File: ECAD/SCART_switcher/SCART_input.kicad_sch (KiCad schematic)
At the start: 12 parts, among them Q1 BC847, Q2 BC847, U1 74AHC1G14

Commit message: progressed ecad
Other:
- note added: "(*1) FUNCTION pin has the following signaling: Level 0: 0 V to +2 V (SCART off) Level 1A: +4.5 V to +7 V (SCART on, 16:9) Level 1B: +9.5 V to +12 V (SCART on) The circuit doesn't distinguish between levels 1A and 1B as these are frequently not respected in consumer products. This way it is simpler to default to 4:3 format and if needed manualy adjust the TV to 16:9."
- note removed: "(*1) FUNCTION pin has the following signaling: Level 0: 0 V to +2 V (SCART off) Level 1A: +4.5 V to +7 V (SCART on, 16:9) Level 1B: +9.5 V to +12 V (SCART on)"
- moved on the sheet: C1, D1, Q1, R2, R3, R?, U1

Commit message: progressed ecad
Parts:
- J?: footprint SCART:SCART-F -> Connector_SCART:SCART-F
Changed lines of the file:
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@@
       (effects (font (size 1.27 1.27)))
     )
-    (property "Footprint" "SCART:SCART-F" (at 90.17 69.85 0)
+    (property "Footprint" "Connector_SCART:SCART-F" (at 90.17 69.85 0)
       (effects (font (size 1.27 1.27)) hide)
     )

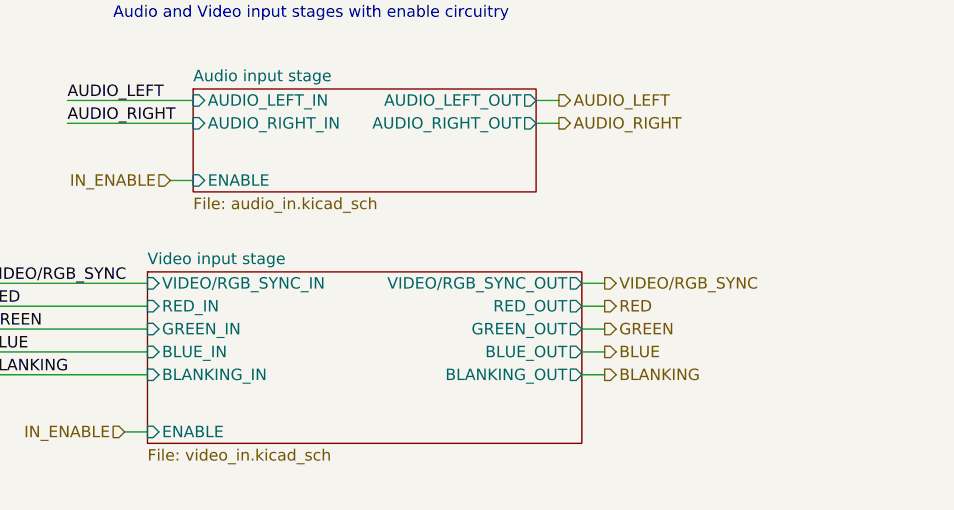
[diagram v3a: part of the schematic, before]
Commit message: ERC fixes.
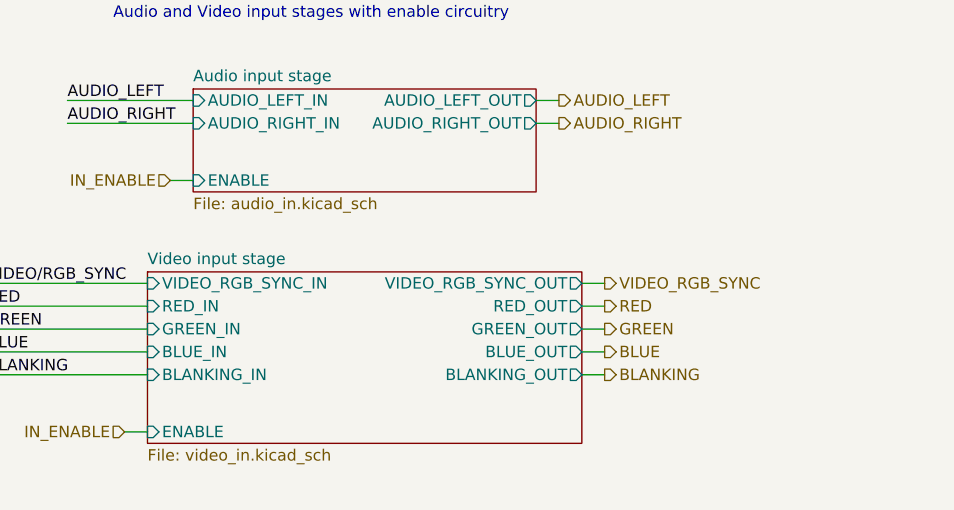
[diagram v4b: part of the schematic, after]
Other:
- sheet Video input stage ports: added VIDEO_RGB_SYNC_IN, VIDEO_RGB_SYNC_OUT; removed VIDEO/RGB_SYNC_IN, VIDEO/RGB_SYNC_OUT
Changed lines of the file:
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@@
     (effects (font (size 1.27 1.27)) (justify left))
   )
-  (hierarchical_label "VIDEO{slash}RGB_SYNC" (shape output) (at 118.11 158.75 0) (fields_autoplaced)
+  (hierarchical_label "VIDEO_RGB_SYNC" (shape output) (at 118.11 158.75 0) (fields_autoplaced)
     (effects (font (size 1.27 1.27)) (justify left))
   )
@@
         (path "/8cd08eb5-4755-4ef5-8eeb-77fd9974b180/f71a1287-269d-4354-9179-cb80a7e1dbca"
           (reference "#PWR0169") (unit 1)
-        )
-      )
-    )
-  )
-  (symbol (lib_id "power:GND") (at 228.6 69.85 0) (unit 1)
-    (in_bom yes) (on_board yes) (dnp no) (fields_autoplaced)
-    (property "Reference" "#PWR012" (at 228.6 76.2 0)
-      (effects (font (size 1.27 1.27)) hide)
-    )
-    (property "Value" "GND" (at 228.6 74.93 0)
-      (effects (font (size 1.27 1.27)))
-    )
-    (property "Footprint" "" (at 228.6 69.85 0)
-      (effects (font (size 1.27 1.27)) hide)
-    )
-    (property "Datasheet" "" (at 228.6 69.85 0)
-      (effects (font (size 1.27 1.27)) hide)
-    )
-    (pin "1")
-    (instances
-      (project "SCART_switcher"
-        (path "/8cd08eb5-4755-4ef5-8eeb-77fd9974b180/6e53f4c9-ed59-4c5d-ac8d-a66f0d353ca7"
-          (reference "#PWR012") (unit 1)
-        )
-        (path "/8cd08eb5-4755-4ef5-8eeb-77fd9974b180/8ea6db35-25d0-43bc-9de5-3ca23502dcdc"
-          (reference "#PWR043") (unit 1)
-        )
-        (path "/8cd08eb5-4755-4ef5-8eeb-77fd9974b180/272a4677-3ef2-418e-abc5-b29f59e726f9"
-          (reference "#PWR059") (unit 1)
-        )
-        (path "/8cd08eb5-4755-4ef5-8eeb-77fd9974b180/56b7edd2-65bf-4844-b6bd-3868b6562f83"
-          (reference "#PWR075") (unit 1)
-        )
-        (path "/8cd08eb5-4755-4ef5-8eeb-77fd9974b180/a066fdde-5f40-4269-95c1-258d611fd7cb"
-          (reference "#PWR091") (unit 1)
-        )
-        (path "/8cd08eb5-4755-4ef5-8eeb-77fd9974b180/ec158eb5-f3e0-409c-b64c-a90e3358941f"
-          (reference "#PWR0107") (unit 1)
-        )
-        (path "/8cd08eb5-4755-4ef5-8eeb-77fd9974b180/6c53b757-b2e6-4d60-b760-4a4a0f832c07"
-          (reference "#PWR0123") (unit 1)
-        )
-        (path "/8cd08eb5-4755-4ef5-8eeb-77fd9974b180/0223a704-ac47-44ed-9ba1-f418acceedb3"
-          (reference "#PWR0139") (unit 1)
-        )
-        (path "/8cd08eb5-4755-4ef5-8eeb-77fd9974b180/2ffa7ecd-d29d-4261-a577-43650ca26099"
-          (reference "#PWR0155") (unit 1)
-        )
-        (path "/8cd08eb5-4755-4ef5-8eeb-77fd9974b180/f71a1287-269d-4354-9179-cb80a7e1dbca"
-          (reference "#PWR0171") (unit 1)
         )
       )
@@
     )
   )
+  (symbol (lib_id "power:GND") (at 228.6 69.85 0) (unit 1)
+    (in_bom yes) (on_board yes) (dnp no) (fields_autoplaced)
+    (property "Reference" "#PWR012" (at 228.6 76.2 0)
+      (effects (font (size 1.27 1.27)) hide)
+    )
+    (property "Value" "GND" (at 228.6 74.93 0)
+      (effects (font (size 1.27 1.27)))
+    )
+    (property "Footprint" "" (at 228.6 69.85 0)
+      (effects (font (size 1.27 1.27)) hide)
+    )
+    (property "Datasheet" "" (at 228.6 69.85 0)
+      (effects (font (size 1.27 1.27)) hide)
+    )
+    (pin "1")
+    (instances
+      (project "SCART_switcher"
+        (path "/8cd08eb5-4755-4ef5-8eeb-77fd9974b180/6e53f4c9-ed59-4c5d-ac8d-a66f0d353ca7"
+          (reference "#PWR012") (unit 1)
+        )
+        (path "/8cd08eb5-4755-4ef5-8eeb-77fd9974b180/8ea6db35-25d0-43bc-9de5-3ca23502dcdc"
+          (reference "#PWR043") (unit 1)
+        )
+        (path "/8cd08eb5-4755-4ef5-8eeb-77fd9974b180/272a4677-3ef2-418e-abc5-b29f59e726f9"
+          (reference "#PWR059") (unit 1)
+        )
+        (path "/8cd08eb5-4755-4ef5-8eeb-77fd9974b180/56b7edd2-65bf-4844-b6bd-3868b6562f83"
+          (reference "#PWR075") (unit 1)
+        )
+        (path "/8cd08eb5-4755-4ef5-8eeb-77fd9974b180/a066fdde-5f40-4269-95c1-258d611fd7cb"
+          (reference "#PWR091") (unit 1)
+        )
+        (path "/8cd08eb5-4755-4ef5-8eeb-77fd9974b180/ec158eb5-f3e0-409c-b64c-a90e3358941f"
+          (reference "#PWR0107") (unit 1)
+        )
+        (path "/8cd08eb5-4755-4ef5-8eeb-77fd9974b180/6c53b757-b2e6-4d60-b760-4a4a0f832c07"
+          (reference "#PWR0123") (unit 1)
+        )
+        (path "/8cd08eb5-4755-4ef5-8eeb-77fd9974b180/0223a704-ac47-44ed-9ba1-f418acceedb3"
+          (reference "#PWR0139") (unit 1)
+        )
+        (path "/8cd08eb5-4755-4ef5-8eeb-77fd9974b180/2ffa7ecd-d29d-4261-a577-43650ca26099"
+          (reference "#PWR0155") (unit 1)
+        )
+        (path "/8cd08eb5-4755-4ef5-8eeb-77fd9974b180/f71a1287-269d-4354-9179-cb80a7e1dbca"
+          (reference "#PWR0171") (unit 1)
+        )
+      )
+    )
+  )
   (symbol (lib_id "power:GND") (at 74.93 45.72 270) (unit 1)
     (in_bom yes) (on_board yes) (dnp no) (fields_autoplaced)
@@
       (effects (font (size 1.27 1.27)) (justify right))
     )
-    (pin "VIDEO{slash}RGB_SYNC_OUT" output (at 115.57 158.75 0)
-      (effects (font (size 1.27 1.27)) (justify right))
-    )
     (pin "GREEN_OUT" output (at 115.57 163.83 0)
       (effects (font (size 1.27 1.27)) (justify right))
@@
       (effects (font (size 1.27 1.27)) (justify right))
     )
-    (pin "VIDEO{slash}RGB_SYNC_IN" input (at 67.31 158.75 180)
-      (effects (font (size 1.27 1.27)) (justify left))
-    )
     (pin "RED_IN" input (at 67.31 161.29 180)
       (effects (font (size 1.27 1.27)) (justify left))
@@
       (effects (font (size 1.27 1.27)) (justify left))
     )
-    (instances
+    (pin "VIDEO_RGB_SYNC_IN" input (at 67.31 158.75 180)
+      (effects (font (size 1.27 1.27)) (justify left))
+    )
+    (pin "VIDEO_RGB_SYNC_OUT" output (at 115.57 158.75 0)
+      (effects (font (size 1.27 1.27)) (justify right))
+    )
+    (instances

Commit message: Progressed ECAD. Error fixing and cleanup.
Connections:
- net VIDEO/RGB_SYNC is gone; now on net VIDEO_RGB_SYNC: J?.20 (P20)

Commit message: Progressed ECAD.
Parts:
- D1: MFN BZX84C3V3LT1G -> (none); MPN (none) -> BZX84C3V3LT1G
- Q1, Q2: MFN BC847B,215 -> (none); MPN (none) -> BC847B,215
- R?: MPN (none) -> RC0805FR-0710KL
- U1: MFN 74AHC1G14SE-7 -> (none); MPN (none) -> 74AHC1G14SE-7
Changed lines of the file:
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@@
       (effects (font (size 1.27 1.27)) (justify left) hide)
     )
-    (property "MFN" "BC847B,215" (at 227.33 140.97 0)
+    (property "MPN" "BC847B,215" (at 227.33 140.97 0)
       (effects (font (size 1.27 1.27)) hide)
     )
@@
       (effects (font (size 1.27 1.27)) hide)
     )
-    (property "MFN" "" (at 218.44 140.97 0)
-      (effects (font (size 1.27 1.27)) hide)
-    )
     (pin "1")
     (pin "2")
@@
       (effects (font (size 1.27 1.27)) hide)
     )
-    (property "MFN" "" (at 264.16 59.69 0)
-      (effects (font (size 1.27 1.27)) hide)
-    )
     (property "MPN" "CL21B104KBCNNNC" (at 264.16 59.69 0)
       (effects (font (size 1.27 1.27)) hide)
@@
     )
     (property "Datasheet" " ~" (at 90.17 69.85 0)
-      (effects (font (size 1.27 1.27)) hide)
-    )
-    (property "MFN" "" (at 90.17 71.12 0)
       (effects (font (size 1.27 1.27)) hide)
     )
@@
       (effects (font (size 1.27 1.27)) hide)
     )
-    (property "MFN" "" (at 229.87 132.08 0)
-      (effects (font (size 1.27 1.27)) hide)
-    )
     (pin "1")
     (pin "2")
@@
       (effects (font (size 1.27 1.27)) hide)
     )
-    (property "MFN" "BZX84C3V3LT1G" (at 191.77 60.96 0)
+    (property "MPN" "BZX84C3V3LT1G" (at 191.77 60.96 0)
       (effects (font (size 1.27 1.27)) hide)
     )
@@
       (effects (font (size 1.27 1.27)) hide)
     )
-    (property "MFN" "74AHC1G14SE-7" (at 233.68 59.69 0)
+    (property "MPN" "74AHC1G14SE-7" (at 233.68 59.69 0)
       (effects (font (size 1.27 1.27)) hide)
     )
@@
       (effects (font (size 1.27 1.27)) (justify left) hide)
     )
-    (property "MFN" "BC847B,215" (at 208.28 64.77 0)
+    (property "MPN" "BC847B,215" (at 208.28 64.77 0)
       (effects (font (size 1.27 1.27)) hide)
     )
@@
       (effects (font (size 1.27 1.27)) hide)
     )
-    (property "MFN" "" (at 191.77 68.58 0)
-      (effects (font (size 1.27 1.27)) hide)
-    )
     (pin "1")
     (pin "2")
@@
       (effects (font (size 1.27 1.27)) hide)
     )
-    (property "Datasheet" "~" (at 191.77 53.34 0)
-      (effects (font (size 1.27 1.27)) hide)
-    )
+    (property "Datasheet" "https://datasheet.lcsc.com/lcsc/1810201611_YAGEO-RC0805FR-0710KL_C84376.pdf" (at 191.77 53.34 0)
+      (effects (font (size 1.27 1.27)) hide)
+    )
+    (property "MPN" "RC0805FR-0710KL" (at 191.77 53.34 0)
+      (effects (font (size 1.27 1.27)) hide)
+    )

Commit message: Progressed ECAD.
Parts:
- C1: footprint Capacitor_SMD:C_0805_2012Metric_Pad1.18x1.45mm_HandSolder -> Capacitor_SMD:C_0805_2012Metric
- R2, R3, R4, R?: footprint Resistor_SMD:R_0805_2012Metric_Pad1.20x1.40mm_HandSolder -> Resistor_SMD:R_0805_2012Metric
- R5: footprint Resistor_SMD:R_1210_3225Metric_Pad1.30x2.65mm_HandSolder -> Resistor_SMD:R_1210_3225Metric
- U1: footprint Package_TO_SOT_SMD:SOT-353_SC-70-5_Handsoldering -> Package_TO_SOT_SMD:SOT-353_SC-70-5
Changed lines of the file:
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@@
       (effects (font (size 1.27 1.27)) (justify left))
     )
-    (property "Footprint" "Resistor_SMD:R_0805_2012Metric_Pad1.20x1.40mm_HandSolder" (at 209.042 55.88 90)
+    (property "Footprint" "Resistor_SMD:R_0805_2012Metric" (at 209.042 55.88 90)
       (effects (font (size 1.27 1.27)) hide)
     )
@@
       (effects (font (size 1.27 1.27)))
     )
-    (property "Footprint" "Resistor_SMD:R_0805_2012Metric_Pad1.20x1.40mm_HandSolder" (at 218.44 142.748 90)
+    (property "Footprint" "Resistor_SMD:R_0805_2012Metric" (at 218.44 142.748 90)
       (effects (font (size 1.27 1.27)) hide)
     )
@@
       (effects (font (size 1.27 1.27)) (justify left))
     )
-    (property "Footprint" "Capacitor_SMD:C_0805_2012Metric_Pad1.18x1.45mm_HandSolder" (at 265.1252 63.5 0)
+    (property "Footprint" "Capacitor_SMD:C_0805_2012Metric" (at 265.1252 63.5 0)
       (effects (font (size 1.27 1.27)) hide)
     )
@@
       (effects (font (size 1.27 1.27)) (justify left))
     )
-    (property "Footprint" "Resistor_SMD:R_1210_3225Metric_Pad1.30x2.65mm_HandSolder" (at 231.648 132.08 90)
+    (property "Footprint" "Resistor_SMD:R_1210_3225Metric" (at 231.648 132.08 90)
       (effects (font (size 1.27 1.27)) hide)
     )
@@
       (effects (font (size 1.27 1.27)))
     )
-    (property "Footprint" "Package_TO_SOT_SMD:SOT-353_SC-70-5_Handsoldering" (at 233.68 59.69 0)
+    (property "Footprint" "Package_TO_SOT_SMD:SOT-353_SC-70-5" (at 233.68 59.69 0)
       (effects (font (size 1.27 1.27)) hide)
     )
@@
       (effects (font (size 1.27 1.27)) (justify left))
     )
-    (property "Footprint" "Resistor_SMD:R_0805_2012Metric_Pad1.20x1.40mm_HandSolder" (at 189.992 68.58 90)
+    (property "Footprint" "Resistor_SMD:R_0805_2012Metric" (at 189.992 68.58 90)
       (effects (font (size 1.27 1.27)) hide)
     )
@@
       (effects (font (size 1.27 1.27)) (justify left))
     )
-    (property "Footprint" "Resistor_SMD:R_0805_2012Metric_Pad1.20x1.40mm_HandSolder" (at 189.992 53.34 90)
-      (effects (font (size 1.27 1.27)) hide)
-    )
+    (property "Footprint" "Resistor_SMD:R_0805_2012Metric" (at 189.992 53.34 90)
+      (effects (font (size 1.27 1.27)) hide)
+    )

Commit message: Progressed ECAD.
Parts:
- D1: MPN BZX84C3V3LT1G -> BZX84C3V3-7-F; Status (none) -> OK
- J?: MPN (none) -> N/A; Status (none) -> OK
- Q1, Q2: MPN BC847B,215 -> BC847C,215; Status (none) -> OK
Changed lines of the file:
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@@
+      (effects (font (size 1.27 1.27)) hide)
+    )
+    (property "Status" "" (at 210.82 55.88 0)
       (effects (font (size 1.27 1.27)) hide)
     )
@@
       (effects (font (size 1.27 1.27) italic) (justify left) hide)
     )
-    (property "Datasheet" "https://datasheet.lcsc.com/lcsc/2304140030_Nexperia-BC847B-215_C57668.pdf" (at 227.33 140.97 0)
+    (property "Datasheet" "https://datasheet.lcsc.com/lcsc/1811141238_Nexperia-BC847C-215_C8664.pdf" (at 227.33 140.97 0)
       (effects (font (size 1.27 1.27)) (justify left) hide)
     )
-    (property "MPN" "BC847B,215" (at 227.33 140.97 0)
+    (property "MPN" "BC847C,215" (at 227.33 140.97 0)
+      (effects (font (size 1.27 1.27)) hide)
+    )
+    (property "Status" "OK" (at 227.33 140.97 0)
       (effects (font (size 1.27 1.27)) hide)
     )
@@
       (effects (font (size 1.27 1.27)) hide)
     )
+    (property "Status" "" (at 218.44 140.97 0)
+      (effects (font (size 1.27 1.27)) hide)
+    )
     (pin "1")
     (pin "2")
@@
     )
     (property "MPN" "333-2SURD/S530-A3" (at 229.87 124.46 0)
+      (effects (font (size 1.27 1.27)) hide)
+    )
+    (property "Status" "" (at 229.87 124.46 0)
       (effects (font (size 1.27 1.27)) hide)
     )
@@
       (effects (font (size 1.27 1.27)) hide)
     )
+    (property "Status" "" (at 264.16 59.69 0)
+      (effects (font (size 1.27 1.27)) hide)
+    )
     (pin "1")
     (pin "2")
@@
     )
     (property "Datasheet" " ~" (at 90.17 69.85 0)
+      (effects (font (size 1.27 1.27)) hide)
+    )
+    (property "Status" "OK" (at 90.17 71.12 0)
+      (effects (font (size 1.27 1.27)) hide)
+    )
+    (property "MPN" "N/A" (at 90.17 71.12 0)
       (effects (font (size 1.27 1.27)) hide)
     )
@@
       (effects (font (size 1.27 1.27)) hide)
     )
+    (property "Status" "" (at 229.87 132.08 0)
+      (effects (font (size 1.27 1.27)) hide)
+    )
     (pin "1")
     (pin "2")
@@
       (effects (font (size 1.27 1.27)) hide)
     )
-    (property "Datasheet" "https://datasheet.lcsc.com/lcsc/2304140030_onsemi-BZX84C3V3LT1G_C82473.pdf" (at 191.77 60.96 0)
-      (effects (font (size 1.27 1.27)) hide)
-    )
-    (property "MPN" "BZX84C3V3LT1G" (at 191.77 60.96 0)
+    (property "Datasheet" "https://datasheet.lcsc.com/lcsc/2304140030_Diodes-Incorporated-BZX84C3V3-7-F_C177019.pdf" (at 191.77 60.96 0)
+      (effects (font (size 1.27 1.27)) hide)
+    )
+    (property "MPN" "BZX84C3V3-7-F" (at 191.77 60.96 0)
+      (effects (font (size 1.27 1.27)) hide)
+    )
+    (property "Status" "OK" (at 191.77 60.96 0)
       (effects (font (size 1.27 1.27)) hide)
     )
@@
       (effects (font (size 1.27 1.27)) hide)
     )
+    (property "Status" "" (at 233.68 59.69 0)
+      (effects (font (size 1.27 1.27)) hide)
+    )
     (pin "3")
     (pin "4")
@@
       (effects (font (size 1.27 1.27) italic) (justify left) hide)
     )
-    (property "Datasheet" "https://datasheet.lcsc.com/lcsc/2304140030_Nexperia-BC847B-215_C57668.pdf" (at 208.28 64.77 0)
+    (property "Datasheet" "https://datasheet.lcsc.com/lcsc/1811141238_Nexperia-BC847C-215_C8664.pdf" (at 208.28 64.77 0)
       (effects (font (size 1.27 1.27)) (justify left) hide)
     )
-    (property "MPN" "BC847B,215" (at 208.28 64.77 0)
+    (property "MPN" "BC847C,215" (at 208.28 64.77 0)
+      (effects (font (size 1.27 1.27)) hide)
+    )
+    (property "Status" "OK" (at 208.28 64.77 0)
       (effects (font (size 1.27 1.27)) hide)
     )
@@
       (effects (font (size 1.27 1.27)) hide)
     )
+    (property "Status" "" (at 191.77 68.58 0)
+      (effects (font (size 1.27 1.27)) hide)
+    )
     (pin "1")
     (pin "2")
@@
       (effects (font (size 1.27 1.27)) hide)
     )
+    (property "Status" "" (at 191.77 53.34 0)
+      (effects (font (size 1.27 1.27)) hide)
+    )
